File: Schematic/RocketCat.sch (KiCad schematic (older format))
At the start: 0 parts

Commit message: Esquematico de Wemos
Denuevo por error de no visualizacion
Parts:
- added U1: WeMos_mini, wemos_d1_mini:D1_mini_board, symbol WeMos_mini
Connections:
- new net LINE: U1.1 (5V), U1.10 (A0), U1.11 (D0), U1.12 (D5), U1.13 (D6), U1.14 (D7), U1.15 (D8), U1.16 (3.3V), U1.2 (GND), U1.3 (D4), U1.4 (D3), U1.5 (D2), U1.6 (D1), U1.7 (Rx), U1.8 (Tx), U1.9 (Rst)

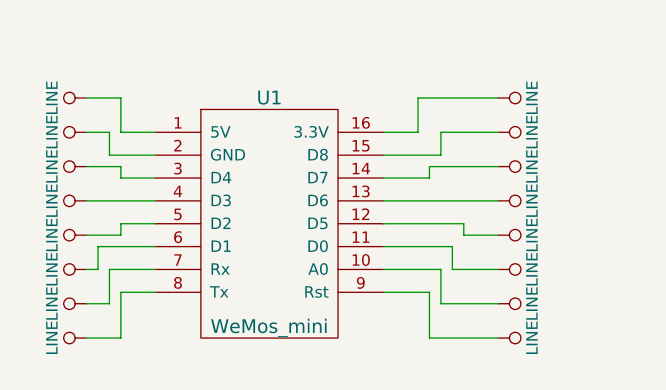
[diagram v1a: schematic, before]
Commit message: Agregado Bateria y gy 87
en lo de la pbc me falta un pista, lo podrias poner pof favor xd
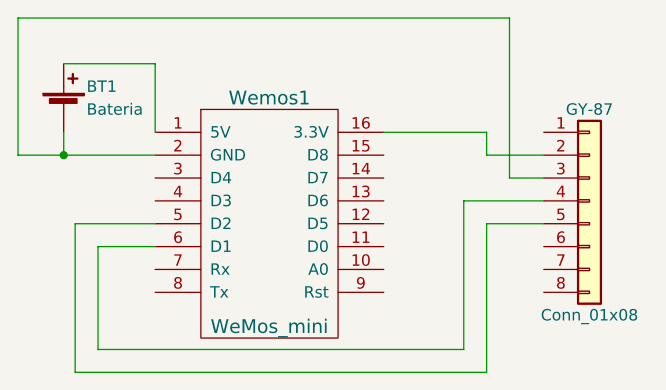
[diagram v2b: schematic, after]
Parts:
- added BT1: Bateria, Battery_Holders:Keystone_1042_1x18650, symbol Battery_Cell
- added GY-87: Conn_01x08, Connectors:Wafer_Horizontal22.5x5.8x7RM2.5-8, symbol Conn_01x08
- renumbered U1 to Wemos1
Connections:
- removed net LINE: Wemos1.1 (5V), Wemos1.10 (A0), Wemos1.11 (D0), Wemos1.12 (D5), Wemos1.13 (D6), Wemos1.14 (D7), Wemos1.15 (D8), Wemos1.16 (3.3V), Wemos1.2 (GND), Wemos1.3 (D4), Wemos1.4 (D3), Wemos1.5 (D2), Wemos1.6 (D1), Wemos1.7 (Rx), Wemos1.8 (Tx), Wemos1.9 (Rst)
- new net: BT1.1 (+), Wemos1.1 (5V)
- new net: GY-87.2 (Pin_2), Wemos1.16 (3.3V)
- new net: BT1.2 (-), GY-87.3 (Pin_3), Wemos1.2 (GND)
- new net: GY-87.5 (Pin_5), Wemos1.5 (D2)
- new net: GY-87.4 (Pin_4), Wemos1.6 (D1)

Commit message: PCB Lista
Checar si no tengo nada mal
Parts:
- removed BT1: Bateria, Battery_Holders:Keystone_1042_1x18650, symbol Battery_Cell
- added D1: LED, LEDs:LED_0805, symbol LED
- added D2: D_Schottky, Diodes_SMD:D_0805, symbol D_Schottky
- added D3: D, Diodes_SMD:D_0805, symbol D
- added J1: Conn_01x08, Socket_Strips:Socket_Strip_Straight_1x08_Pitch2.54mm, symbol Conn_01x08
- added J2: Conn_01x02, Socket_Strips:Socket_Strip_Straight_1x02_Pitch2.54mm, symbol Conn_01x02
- added R1: 1k, Resistors_SMD:R_0805, symbol R
- added R2: 10K, Resistors_SMD:R_0805, symbol R
- added U1: MCP73831T-4ADI/OT, TO_SOT_Packages_SMD:SOT-23-5, symbol MCP73831T-4ADI/OT
- GY-87: footprint Connectors:Wafer_Horizontal22.5x5.8x7RM2.5-8 -> Socket_Strips:Socket_Strip_Straight_1x08_Pitch2.54mm
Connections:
- net VCC: now reaches Wemos1.1 (5V)
- net VCC: now also D1.2 (A), D2.1 (K), U1.4 (VDD)
- net A0: now reaches Wemos1.10 (A0)
- net A0: now also J1.1 (Pin_1)
- net D0: now reaches Wemos1.11 (D0)
- net D0: now also J1.2 (Pin_2)
- net D5: now reaches Wemos1.12 (D5)
- net D5: now also J1.6 (Pin_6)
- net D6: now reaches Wemos1.13 (D6)
- net D6: now also J1.5 (Pin_5)
- net D7: now reaches Wemos1.14 (D7)
- net D7: now also J1.4 (Pin_4)
- net D8: now reaches Wemos1.15 (D8)
- net D8: now also J1.3 (Pin_3)
- net +3V3: now reaches GY-87.2 (Pin_2), Wemos1.16 (3.3V)
- net GND: now reaches GY-87.3 (Pin_3), Wemos1.2 (GND)
- net GND: now also J2.2 (Pin_2), R1.2, U1.2 (VSS)
- net D4: now reaches Wemos1.3 (D4)
- net D4: now also J1.7 (Pin_7)
- net D3: now reaches Wemos1.4 (D3)
- net D3: now also J1.8 (Pin_8)
- net D2: now reaches GY-87.5 (Pin_5), Wemos1.5 (D2)
- net D1: now reaches GY-87.4 (Pin_4), Wemos1.6 (D1)
- new net: R2.2, U1.1 (STAT)
- new net: R1.1, U1.5 (PROG)
- new net: D1.1 (K), R2.1
- new net +BATT: D2.2 (A), D3.1 (K), D3.2 (A), J2.1 (Pin_1), U1.3 (VBAT)
- no-connect marks 0 -> 7
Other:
- moved on the sheet: GY-87

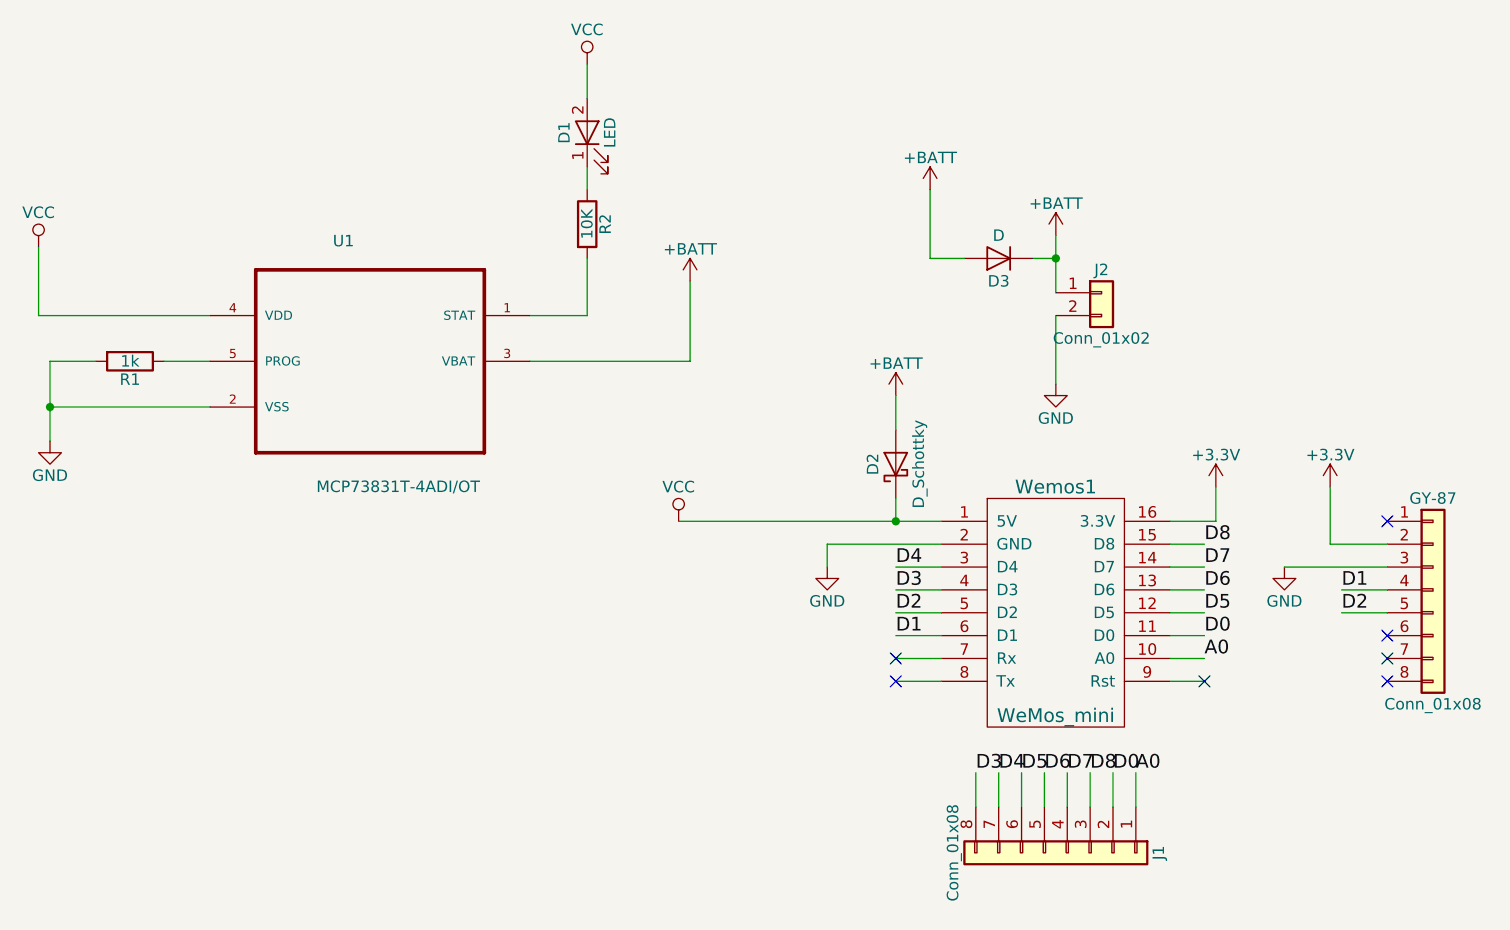
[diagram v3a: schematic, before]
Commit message: fix size and tracks remove MCP charger
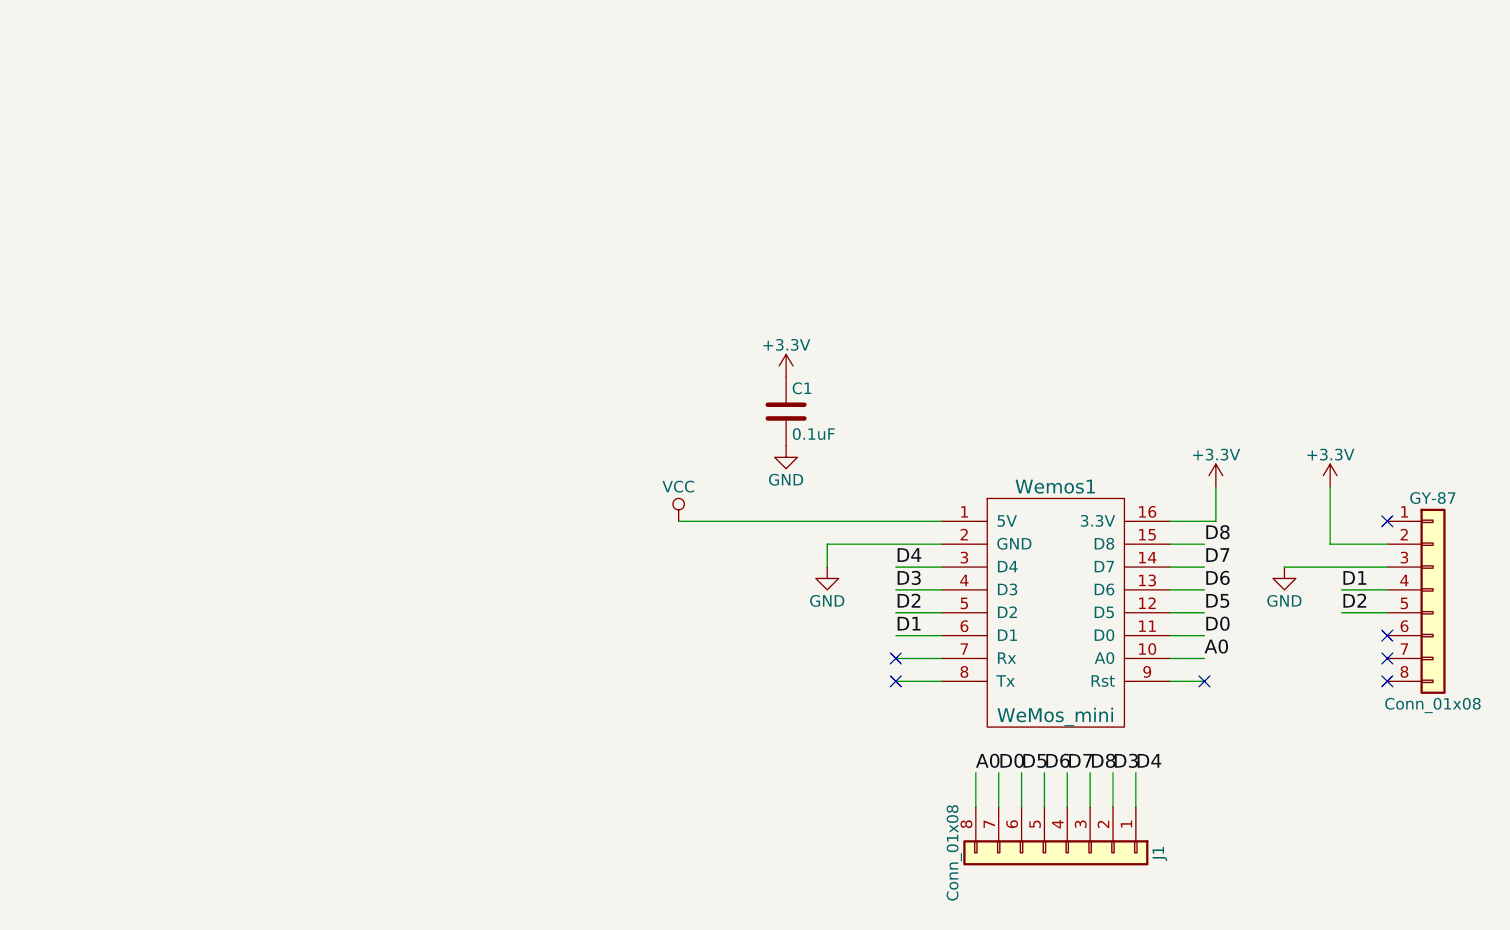
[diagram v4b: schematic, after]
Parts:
- removed D1: LED, LEDs:LED_0805, symbol LED
- removed D2: D_Schottky, Diodes_SMD:D_0805, symbol D_Schottky
- removed D3: D, Diodes_SMD:D_0805, symbol D
- removed J2: Conn_01x02, Socket_Strips:Socket_Strip_Straight_1x02_Pitch2.54mm, symbol Conn_01x02
- removed R1: 1k, Resistors_SMD:R_0805, symbol R
- removed R2: 10K, Resistors_SMD:R_0805, symbol R
- removed U1: MCP73831T-4ADI/OT, TO_SOT_Packages_SMD:SOT-23-5, symbol MCP73831T-4ADI/OT
- added C1: 0.1uF, symbol C
- Wemos1: footprint wemos_d1_mini:D1_mini_board -> wemos-d1-mini:wemos-d1-mini-connectors-only
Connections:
- net +3V3: now also C1.1
- net A0: now also J1.8 (Pin_8); no longer J1.1 (Pin_1)
- net D0: now also J1.7 (Pin_7); no longer J1.2 (Pin_2)
- net D3: now also J1.2 (Pin_2); no longer J1.8 (Pin_8)
- net D4: now also J1.1 (Pin_1); no longer J1.7 (Pin_7)
- net GND: now also C1.2
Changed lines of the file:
@@
 LIBS:contrib
 LIBS:valves
-LIBS:wemos_mini
-LIBS:MCP73831T-4ADI_OT
 LIBS:RocketCat-cache
 EELAYER 25 0
@@
 F 0 "Wemos1" H 5450 3500 60  0000 C CNN
 F 1 "WeMos_mini" H 5450 2500 60  0000 C CNN
-F 2 "wemos_d1_mini:D1_mini_board" H 6000 2300 60  0001 C CNN
+F 2 "wemos-d1-mini:wemos-d1-mini-connectors-only" H 6000 2300 60  0001 C CNN
 F 3 "" H 6000 2300 60  0000 C CNN
 	1    5450 3000
@@
 Wire Wire Line
 	5100 3750 5100 3900
-Text Label 5100 3750 0    60   ~ 0
+Text Label 5700 3750 0    60   ~ 0
 D3
-Text Label 5200 3750 0    60   ~ 0
+Text Label 5800 3750 0    60   ~ 0
 D4
 Text Label 5300 3750 0    60   ~ 0
@@
 Text Label 5600 3750 0    60   ~ 0
 D8
-Text Label 5700 3750 0    60   ~ 0
+Text Label 5200 3750 0    60   ~ 0
 D0
-Text Label 5800 3750 0    60   ~ 0
+Text Label 5100 3750 0    60   ~ 0
 A0
 Wire Wire Line
-	5450 1400 5450 1650
-Wire Wire Line
-	5450 1750 5450 2050
-$Comp
-L MCP73831T-4ADI/OT U1
-U 1 1 5A57B270
-P 2450 1850
-F 0 "U1" H 2287 2247 50  0000 L BNN
-F 1 "MCP73831T-4ADI/OT" H 2215 1172 50  0000 L BNN
-F 2 "TO_SOT_Packages_SMD:SOT-23-5" H 2450 1850 50  0001 L BNN
-F 3 "0.46 USD" H 2450 1850 50  0001 L BNN
-F 4 "SOT-23-5 Microchip" H 2450 1850 50  0001 L BNN "Campo4"
-F 5 "Microchip" H 2450 1850 50  0001 L BNN "Campo5"
-F 6 "Good" H 2450 1850 50  0001 L BNN "Campo6"
-F 7 "IC CONTRLR LI-ION 4.40V SOT23-5" H 2450 1850 50  0001 L BNN "Campo7"
-F 8 "MCP73831T-4ADI/OT" H 2450 1850 50  0001 L BNN "Campo8"
-	1    2450 1850
-	1    0    0    -1
-$EndComp
-$Comp
-L LED D1
-U 1 1 5A57B422
-P 3400 950
-F 0 "D1" H 3400 1050 50  0000 C CNN
-F 1 "LED" H 3400 850 50  0000 C CNN
-F 2 "LEDs:LED_0805" H 3400 950 50  0001 C CNN
-F 3 "" H 3400 950 50  0001 C CNN
-	1    3400 950
-	0    -1   -1   0
-$EndComp
-$Comp
-L R R2
-U 1 1 5A57B461
-P 3400 1350
-F 0 "R2" V 3480 1350 50  0000 C CNN
-F 1 "10K" V 3400 1350 50  0000 C CNN
-F 2 "Resistors_SMD:R_0805" V 3330 1350 50  0001 C CNN
-F 3 "" H 3400 1350 50  0001 C CNN
-	1    3400 1350
-	1    0    0    -1
-$EndComp
-Wire Wire Line
-	3400 1200 3400 1100
-Wire Wire Line
-	3400 1500 3400 1750
-Wire Wire Line
-	3400 1750 3150 1750
-Wire Wire Line
-	1750 1750 1000 1750
-Wire Wire Line
-	1000 1750 1000 1450
-Wire Wire Line
-	3400 800  3400 650
-$Comp
-L R R1
-U 1 1 5A57BA30
-P 1400 1950
-F 0 "R1" V 1480 1950 50  0000 C CNN
-F 1 "1k" V 1400 1950 50  0000 C CNN
-F 2 "Resistors_SMD:R_0805" V 1330 1950 50  0001 C CNN
-F 3 "" H 1400 1950 50  0001 C CNN
-	1    1400 1950
-	0    1    1    0
-$EndComp
-Wire Wire Line
-	1750 1950 1550 1950
-Wire Wire Line
-	1750 2150 1050 2150
-Wire Wire Line
-	1050 1950 1050 2300
-Wire Wire Line
-	1050 1950 1250 1950
-Connection ~ 1050 2150
-$Comp
-L GND #PWR05
-U 1 1 5A57BB5C
-P 1050 2300
-F 0 "#PWR05" H 1050 2050 50  0001 C CNN
-F 1 "GND" H 1050 2150 50  0000 C CNN
-F 2 "" H 1050 2300 50  0001 C CNN
-F 3 "" H 1050 2300 50  0001 C CNN
-	1    1050 2300
-	1    0    0    -1
-$EndComp
-Wire Wire Line
-	3150 1950 3850 1950
-Wire Wire Line
-	3850 1950 3850 1600
-$Comp
-L +BATT #PWR06
-U 1 1 5A57BCD0
-P 3850 1600
-F 0 "#PWR06" H 3850 1450 50  0001 C CNN
-F 1 "+BATT" H 3850 1740 50  0000 C CNN
-F 2 "" H 3850 1600 50  0001 C CNN
-F 3 "" H 3850 1600 50  0001 C CNN
-	1    3850 1600
-	1    0    0    -1
-$EndComp
-$Comp
-L GND #PWR07
-U 1 1 5A57BF04
-P 5450 2050
-F 0 "#PWR07" H 5450 1800 50  0001 C CNN
-F 1 "GND" H 5450 1900 50  0000 C CNN
-F 2 "" H 5450 2050 50  0001 C CNN
-F 3 "" H 5450 2050 50  0001 C CNN
-	1    5450 2050
-	1    0    0    -1
-$EndComp
-$Comp
-L +BATT #PWR08
-U 1 1 5A57C816
-P 4900 1200
-F 0 "#PWR08" H 4900 1050 50  0001 C CNN
-F 1 "+BATT" H 4900 1340 50  0000 C CNN
-F 2 "" H 4900 1200 50  0001 C CNN
-F 3 "" H 4900 1200 50  0001 C CNN
-	1    4900 1200
-	1    0    0    -1
-$EndComp
-$Comp
-L D D3
-U 1 1 5A57C83C
-P 5200 1500
-F 0 "D3" H 5200 1600 50  0000 C CNN
-F 1 "D" H 5200 1400 50  0000 C CNN
-F 2 "Diodes_SMD:D_0805" H 5200 1500 50  0001 C CNN
-F 3 "" H 5200 1500 50  0001 C CNN
-	1    5200 1500
-	-1   0    0    1
-$EndComp
-Wire Wire Line
-	5050 1500 4900 1500
-Wire Wire Line
-	4900 1500 4900 1200
-Wire Wire Line
-	5350 1500 5450 1500
-Connection ~ 5450 1500
-$Comp
-L D_Schottky D2
-U 1 1 5A57D65B
-P 4750 2400
-F 0 "D2" H 4750 2500 50  0000 C CNN
-F 1 "D_Schottky" H 4750 2300 50  0000 C CNN
-F 2 "Diodes_SMD:D_0805" H 4750 2400 50  0001 C CNN
-F 3 "" H 4750 2400 50  0001 C CNN
-	1    4750 2400
-	0    -1   -1   0
-$EndComp
-Wire Wire Line
 	4950 2650 3800 2650
-Wire Wire Line
-	4750 2550 4750 2650
-Connection ~ 4750 2650
-Wire Wire Line
-	4750 2250 4750 2100
-$Comp
-L VCC #PWR09
+$Comp
+L VCC #PWR05
 U 1 1 5A57DA3C
 P 3800 2650
-F 0 "#PWR09" H 3800 2500 50  0001 C CNN
+F 0 "#PWR05" H 3800 2500 50  0001 C CNN
 F 1 "VCC" H 3800 2800 50  0000 C CNN
 F 2 "" H 3800 2650 50  0001 C CNN
@@
 $EndComp
 $Comp
-L VCC #PWR010
-U 1 1 5A57DAAA
-P 1000 1450
-F 0 "#PWR010" H 1000 1300 50  0001 C CNN
-F 1 "VCC" H 1000 1600 50  0000 C CNN
-F 2 "" H 1000 1450 50  0001 C CNN
-F 3 "" H 1000 1450 50  0001 C CNN
-	1    1000 1450
-	1    0    0    -1
-$EndComp
-$Comp
-L VCC #PWR011
-U 1 1 5A57DAD2
-P 3400 650
-F 0 "#PWR011" H 3400 500 50  0001 C CNN
-F 1 "VCC" H 3400 800 50  0000 C CNN
-F 2 "" H 3400 650 50  0001 C CNN
-F 3 "" H 3400 650 50  0001 C CNN
-	1    3400 650
-	1    0    0    -1
-$EndComp
-$Comp
-L +BATT #PWR012
-U 1 1 5A57DB0E
-P 5450 1400
-F 0 "#PWR012" H 5450 1250 50  0001 C CNN
-F 1 "+BATT" H 5450 1540 50  0000 C CNN
-F 2 "" H 5450 1400 50  0001 C CNN
-F 3 "" H 5450 1400 50  0001 C CNN
-	1    5450 1400
-	1    0    0    -1
-$EndComp
-$Comp
-L +BATT #PWR013
-U 1 1 5A57DB36
-P 4750 2100
-F 0 "#PWR013" H 4750 1950 50  0001 C CNN
-F 1 "+BATT" H 4750 2240 50  0000 C CNN
-F 2 "" H 4750 2100 50  0001 C CNN
-F 3 "" H 4750 2100 50  0001 C CNN
-	1    4750 2100
-	1    0    0    -1
-$EndComp
-$Comp
-L Conn_01x02 J2
-U 1 1 5A57DE30
-P 5650 1650
-F 0 "J2" H 5650 1750 50  0000 C CNN
-F 1 "Conn_01x02" H 5650 1450 50  0000 C CNN
-F 2 "Socket_Strips:Socket_Strip_Straight_1x02_Pitch2.54mm" H 5650 1650 50  0001 C CNN
-F 3 "" H 5650 1650 50  0001 C CNN
-	1    5650 1650
-	1    0    0    -1
-$EndComp
+L C C1
+U 1 1 5A61147F
+P 4270 2170
+F 0 "C1" H 4295 2270 50  0000 L CNN
+F 1 "0.1uF" H 4295 2070 50  0000 L CNN
+F 2 "" H 4308 2020 50  0001 C CNN
+F 3 "" H 4270 2170 50  0001 C CNN
+	1    4270 2170
+	1    0    0    -1
+$EndComp
+$Comp
+L +3.3V #PWR?
+U 1 1 5A6114D1
+P 4270 2020
+F 0 "#PWR?" H 4270 1870 50  0001 C CNN
+F 1 "+3.3V" H 4270 2160 50  0000 C CNN
+F 2 "" H 4270 2020 50  0001 C CNN
+F 3 "" H 4270 2020 50  0001 C CNN
+	1    4270 2020
+	1    0    0    -1
+$EndComp
+$Comp
+L GND #PWR?
+U 1 1 5A6114EC
+P 4270 2320
+F 0 "#PWR?" H 4270 2070 50  0001 C CNN
+F 1 "GND" H 4270 2170 50  0000 C CNN
+F 2 "" H 4270 2320 50  0001 C CNN
+F 3 "" H 4270 2320 50  0001 C CNN
+	1    4270 2320
+	1    0    0    -1
+$EndComp
